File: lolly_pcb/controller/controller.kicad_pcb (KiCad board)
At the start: 2 copper layers, 93.8 x 60.6 mm, 120 parts, among them J1 Conn_01x02_Pin, SW1 SW_SPDT, U1 ESP32-S2-MINI-1

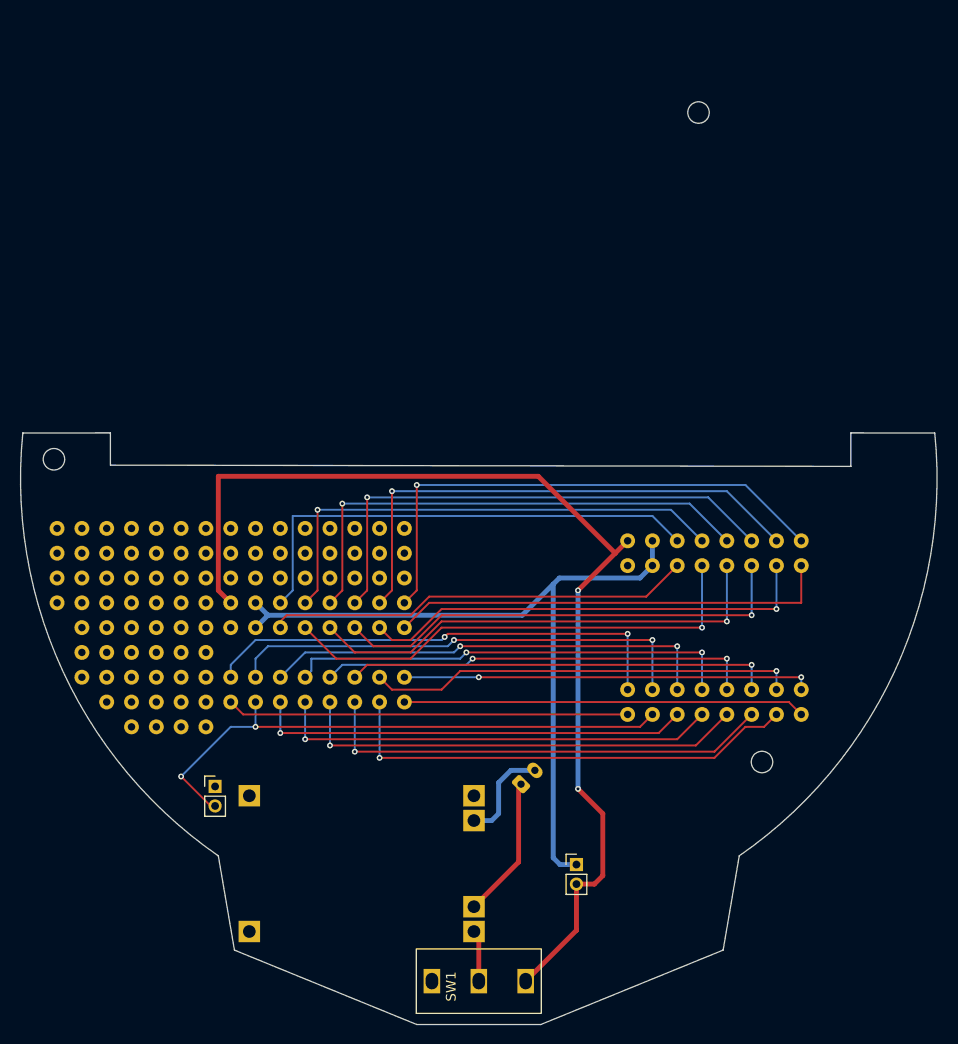
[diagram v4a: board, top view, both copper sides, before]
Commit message: rearrange board for usb-c breakout board
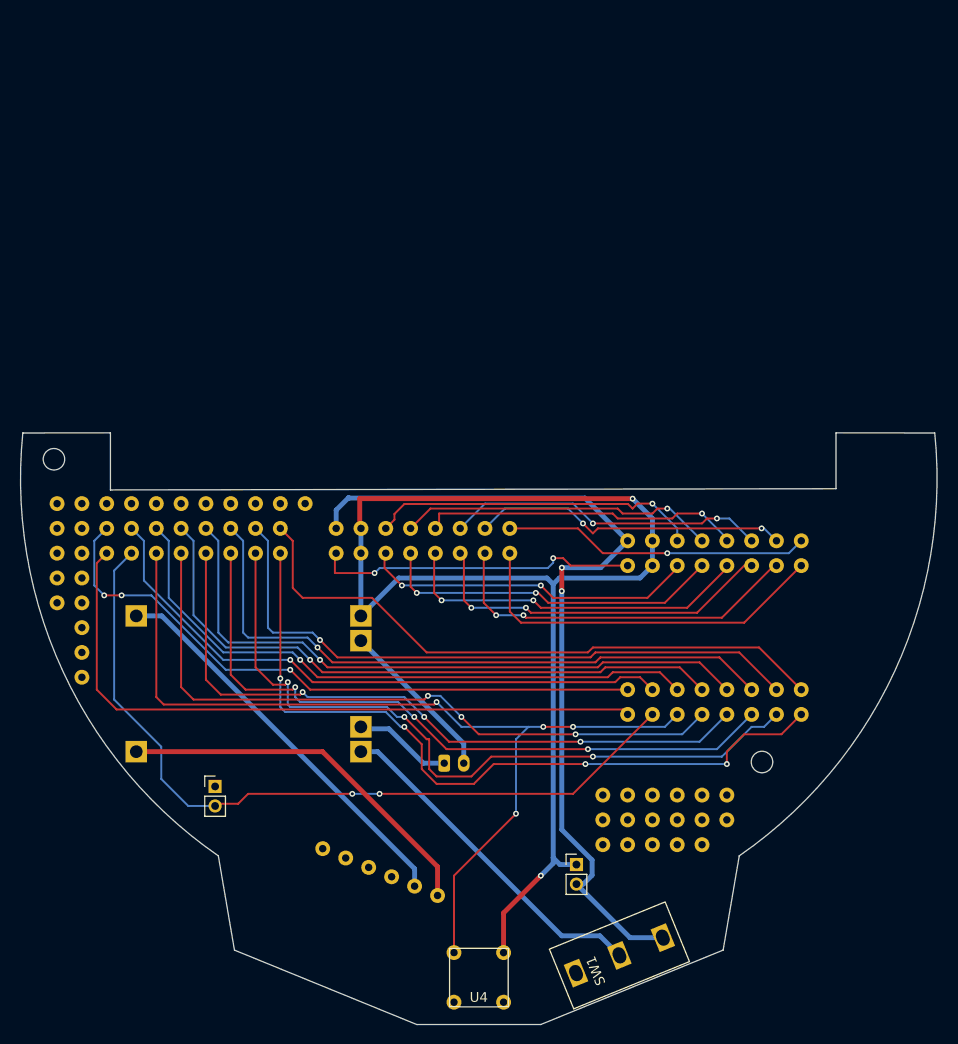
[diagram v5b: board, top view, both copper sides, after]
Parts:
- removed the ? at (124.6, 110.2)
- removed the ? at (122.1, 120.3)
- removed the ? at (122.1, 122.9)
- removed the ? at (117.0, 117.8)
- removed the ? at (124.6, 107.6)
- removed the ? at (114.4, 122.9)
- removed the ? at (111.9, 117.8)
- removed the ? at (119.5, 120.3)
- removed the ? at (132.2, 107.6)
- removed the ? at (117.0, 107.6)
- removed the ? at (122.1, 107.6)
- removed the ? at (137.3, 107.6)
- removed the ? at (129.7, 107.6)
- removed the ? at (129.7, 105.1)
- removed the ? at (111.9, 122.9)
- removed the ? at (127.1, 107.6)
- removed the ? at (111.9, 112.7)
- removed the ? at (127.1, 105.1)
- removed the ? at (119.5, 115.2)
- removed the ? at (124.6, 105.1)
- removed the ? at (117.0, 125.4)
- removed the ? at (139.8, 110.2)
- removed the ? at (122.1, 115.2)
- removed the ? at (127.1, 110.2)
- removed the ? at (122.1, 112.7)
- removed the ? at (122.1, 125.4)
- removed the ? at (134.8, 107.6)
- removed the ? at (129.7, 110.2)
- removed the ? at (117.0, 112.7)
- removed the ? at (139.8, 105.1)
- removed the ? at (114.4, 107.6)
- removed the ? at (114.4, 117.8)
- removed the ? at (119.5, 107.6)
- removed the ? at (142.4, 105.1)
- removed the ? at (114.4, 112.7)
- removed the ? at (119.5, 122.9)
- removed the ? at (137.3, 110.2)
- removed the ? at (119.5, 110.2)
- removed the ? at (119.5, 125.4)
- removed the ? at (132.2, 105.1)
- removed the ? at (114.4, 110.2)
- removed the ? at (142.4, 110.2)
- removed the ? at (117.0, 120.3)
- removed the ? at (117.0, 105.1)
- removed the ? at (119.5, 117.8)
- removed the ? at (142.4, 107.6)
- removed the ? at (139.8, 107.6)
- removed the ? at (117.0, 122.9)
- removed the ? at (119.5, 105.1)
- removed the ? at (119.5, 112.7)
- removed the ? at (114.4, 115.2)
- removed the ? at (111.9, 107.6)
- removed the ? at (111.9, 115.2)
- removed the ? at (117.0, 115.2)
- removed the ? at (114.4, 125.4)
- removed the ? at (134.8, 105.1)
- removed the ? at (111.9, 120.3)
- removed the ? at (137.3, 105.1)
- removed the ? at (122.1, 105.1)
- removed the ? at (134.8, 110.2)
- removed the ? at (132.2, 110.2)
- removed the ? at (117.0, 110.2)
- removed the ? at (114.4, 105.1)
- removed the ? at (111.9, 105.1)
- removed the ? at (122.1, 117.8)
- removed the ? at (114.4, 120.3)
- removed the ? at (111.9, 110.2)
- removed the ? at (122.1, 110.2)
- removed the REF** at (172.5, 62.5)
- added ?: , , F.Cu at (170.3, 134.9)
- added ?: , , F.Cu at (175.4, 132.4)
- added ?: , , F.Cu at (162.7, 134.9)
- added ?: , , F.Cu at (175.4, 134.9)
- added ?: , , F.Cu at (167.8, 137.5)
- added ?: , , F.Cu at (165.2, 132.4)
- added ?: , , F.Cu at (127.1, 102.5)
- added ?: , , F.Cu at (111.9, 102.5)
- added ?: , , F.Cu at (162.7, 137.5)
- added ?: , , F.Cu at (165.2, 134.9)
- added ?: , , F.Cu at (119.5, 102.5)
- added ?: , , F.Cu at (129.7, 102.5)
- added ?: , , F.Cu at (165.2, 137.5)
- added ?: , , F.Cu at (124.6, 102.5)
- added ?: , , F.Cu at (167.8, 134.9)
- added ?: , , F.Cu at (172.9, 137.5)
- added ?: , , F.Cu at (109.4, 102.5)
- added ?: , , F.Cu at (106.8, 102.5)
- added ?: , , F.Cu at (172.9, 134.9)
- added ?: , , F.Cu at (172.9, 132.4)
- added ?: , , F.Cu at (122.1, 102.5)
- added ?: , , F.Cu at (162.7, 132.4)
- added ?: , , F.Cu at (132.2, 102.5)
- added ?: , , F.Cu at (167.8, 132.4)
- added ?: , , F.Cu at (117.0, 102.5)
- added ?: , , F.Cu at (170.3, 137.5)
- added ?: , , F.Cu at (114.4, 102.5)
- added ?: , , F.Cu at (170.3, 132.4)
- added U3: ~, controller:usb-c 5v breakout, B.Cu at (135.1, 152.0)
- added U4: ~, controller:small thoughhole button, F.Cu at (150.0, 153.6)
- moved U2 21.8 mm to (114.9, 127.9)
- moved ? 19.8 mm to (124.6, 105.1)
- moved ? 19.8 mm to (124.6, 107.6)
- moved ? 19.8 mm to (119.5, 105.1)
- moved ? 19.8 mm to (114.4, 105.1)
- moved ? 19.8 mm to (127.1, 105.1)
- moved ? 19.8 mm to (114.4, 107.6)
- moved ? 19.8 mm to (117.0, 105.1)
- moved ? 19.8 mm to (117.0, 107.6)
- moved ? 19.8 mm to (127.1, 107.6)
- moved ? 19.8 mm to (119.5, 107.6)
- moved ? 19.8 mm to (122.1, 107.6)
- moved ? 19.8 mm to (111.9, 107.6)
- moved ? 19.8 mm to (111.9, 105.1)
- moved ? 19.8 mm to (129.7, 107.6)
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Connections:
- U2 pad 1: unconnected-(U2-In_+-Pad1) -> Net-(U2-In_+)
- U2 pad 2: unconnected-(U2-In_--Pad2) -> Net-(U2-In_-)
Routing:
- net 11: track 44.6 -> 96.3 mm, vias 1 -> 4
- net GND: track 78.3 -> 122.5 mm, vias 0 -> 2
- net Net-(U2-In_-): track 0.00 -> 41.0 mm
- net Net-(U2-In_+): track 0.00 -> 38.7 mm
- net EN: track 41.2 -> 77.5 mm, vias 0 -> 4
- net 15: track 0.00 -> 33.1 mm, vias 0 -> 2
- net Net-(SW1-B): track 4.59 -> 35.1 mm
- net 3V3: track 41.2 -> 69.8 mm
- net 3: track 48.2 -> 75.6 mm, vias 1 -> 3
- net 9: track 45.5 -> 70.2 mm, vias 1 -> 3
- net 5: track 47.3 -> 71.2 mm, vias 1 -> 3
- net 7: track 46.4 -> 70.3 mm, vias 1 -> 3
- net 12: track 57.7 -> 80.8 mm
- net 39: track 54.3 -> 31.4 mm
- net 4: track 43.7 -> 66.1 mm
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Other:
- outline, holes or cut-outs redrawn

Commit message: add labels
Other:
- board text added: "1"
- board text added: "10"
- board text added: "11"
- board text added: "12"
- board text added: "13"
- board text added: "14"
- board text added: "15"
- board text added: "16"
- board text added: "17"
- board text added: "18"
- board text added: "2"
- board text added: "21"
- board text added: "3"
- board text added: "33"
- board text added: "34"
- board text added: "35"
- board text added: "36"
- board text added: "37"
- board text added: "38"
- board text added: "39"
- board text added: "3V3"
- board text added: "4"
- board text added: "40"
- board text added: "5"
- board text added: "6"
- board text added: "7"
- board text added: "8"
- board text added: "9"
- board text added: "EN"
- board text added: "GND"
- board text added: "Mini Lolly Controller V1"
- board text added: "VBUS"
